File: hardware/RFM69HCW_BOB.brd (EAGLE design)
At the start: 27.9 x 20.3 mm, 11 parts, among them U1 RFM69HCW

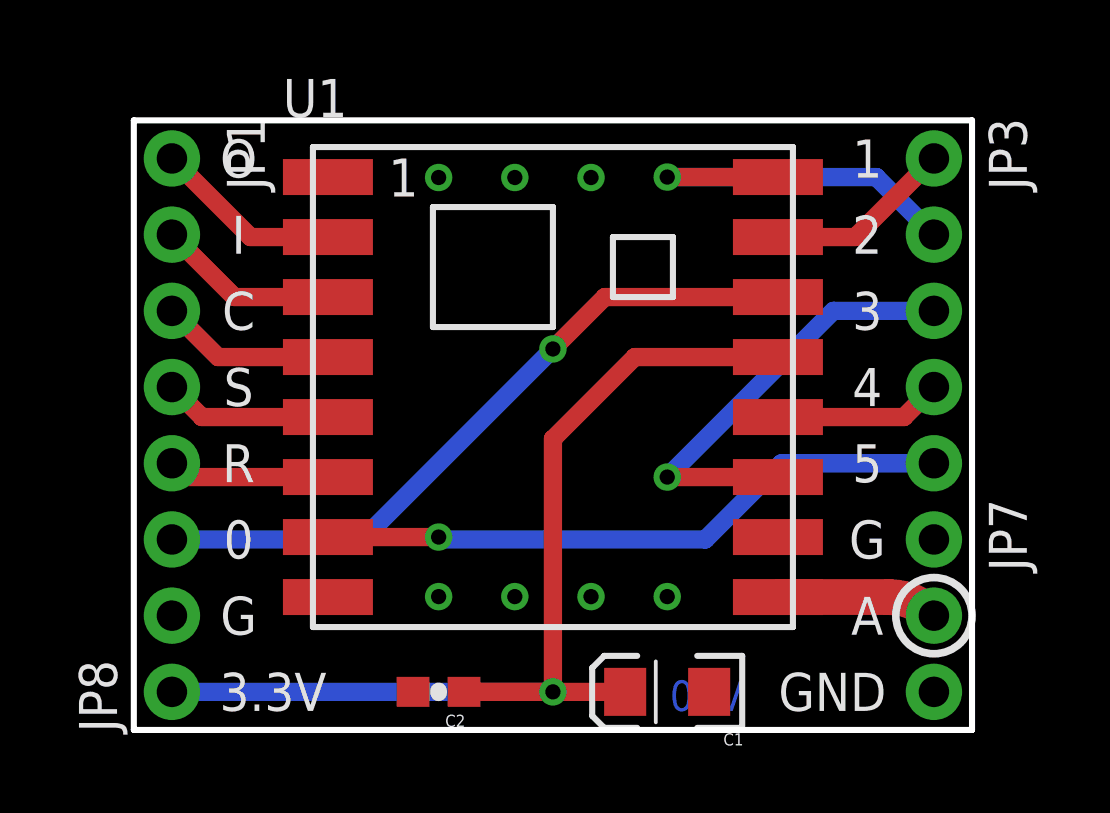
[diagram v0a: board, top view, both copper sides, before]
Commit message: Added fiducials to HCW BOB, initial example code
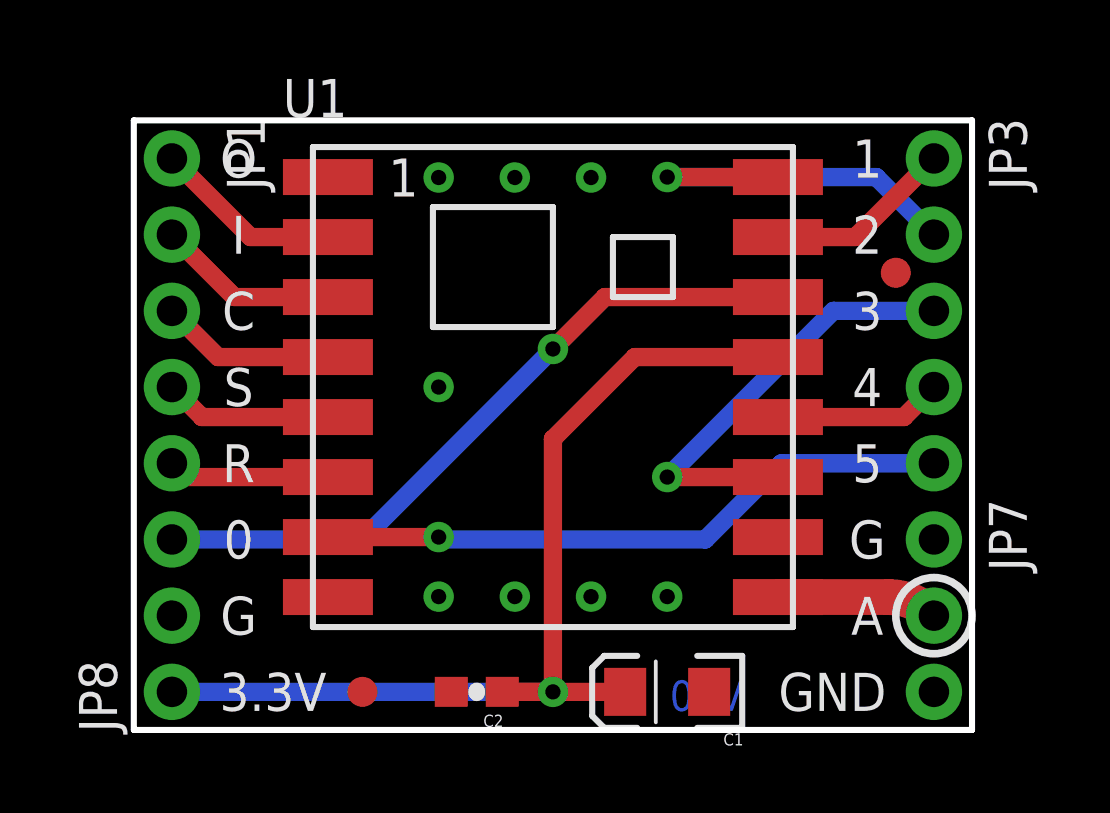
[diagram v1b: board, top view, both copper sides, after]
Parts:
- added FID1, FID2: FIDUCIAL1X2, SparkFun-Aesthetics:FIDUCIAL-1X2
- moved C2 1.27 mm to (11.4, 1.27)
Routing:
- net 3.3V: track 35.1 -> 33.9 mm
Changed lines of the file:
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@@
 <?xml version="1.0" encoding="utf-8"?>
 <!DOCTYPE eagle SYSTEM "eagle.dtd">
-<eagle version="6.4">
+<eagle version="6.5.0">
 <drawing>
 <settings>
@@
 <grid distance="0.05" unitdist="inch" unit="inch" style="lines" multiple="2" display="yes" altdistance="0.0125" altunitdist="inch" altunit="inch"/>
 <layers>
-<layer number="1" name="Top" color="4" fill="1" visible="no" active="yes"/>
+<layer number="1" name="Top" color="4" fill="1" visible="yes" active="yes"/>
 <layer number="2" name="Route2" color="1" fill="3" visible="no" active="no"/>
 <layer number="3" name="Route3" color="4" fill="3" visible="no" active="no"/>
@@
 <layer number="14" name="Route14" color="1" fill="6" visible="no" active="no"/>
 <layer number="15" name="Route15" color="4" fill="6" visible="no" active="no"/>
-<layer number="16" name="Bottom" color="1" fill="1" visible="yes" active="yes"/>
+<layer number="16" name="Bottom" color="1" fill="1" visible="no" active="yes"/>
 <layer number="17" name="Pads" color="2" fill="1" visible="yes" active="yes"/>
 <layer number="18" name="Vias" color="2" fill="1" visible="yes" active="yes"/>
 <layer number="19" name="Unrouted" color="6" fill="1" visible="yes" active="yes"/>
 <layer number="20" name="Dimension" color="15" fill="1" visible="yes" active="yes"/>
-<layer number="21" name="tPlace" color="7" fill="1" visible="no" active="yes"/>
-<layer number="22" name="bPlace" color="7" fill="1" visible="yes" active="yes"/>
-<layer number="23" name="tOrigins" color="15" fill="1" visible="no" active="yes"/>
-<layer number="24" name="bOrigins" color="15" fill="1" visible="yes" active="yes"/>
+<layer number="21" name="tPlace" color="7" fill="1" visible="yes" active="yes"/>
+<layer number="22" name="bPlace" color="7" fill="1" visible="no" active="yes"/>
+<layer number="23" name="tOrigins" color="15" fill="1" visible="yes" active="yes"/>
+<layer number="24" name="bOrigins" color="15" fill="1" visible="no" active="yes"/>
 <layer number="25" name="tNames" color="7" fill="1" visible="no" active="yes"/>
 <layer number="26" name="bNames" color="7" fill="1" visible="no" active="yes"/>
 <layer number="27" name="tValues" color="7" fill="1" visible="no" active="yes"/>
 <layer number="28" name="bValues" color="7" fill="1" visible="no" active="yes"/>
-<layer number="29" name="tStop" color="7" fill="3" visible="no" active="yes"/>
+<layer number="29" name="tStop" color="7" fill="3" visible="yes" active="yes"/>
 <layer number="30" name="bStop" color="7" fill="6" visible="no" active="yes"/>
-<layer number="31" name="tCream" color="7" fill="4" visible="no" active="yes"/>
+<layer number="31" name="tCream" color="7" fill="4" visible="yes" active="yes"/>
 <layer number="32" name="bCream" color="7" fill="5" visible="no" active="yes"/>
 <layer number="33" name="tFinish" color="6" fill="3" visible="no" active="yes"/>
@@
 </class>
 </classes>
-<designrules name="default *">
-<description language="de">&lt;b&gt;EAGLE Design Rules&lt;/b&gt;
-&lt;p&gt;
-Die Standard-Design-Rules sind so gewählt, dass sie für
-die meisten Anwendungen passen. Sollte ihre Platine
-besondere Anforderungen haben, treffen Sie die erforderlichen
-Einstellungen hier und speichern die Design Rules unter
-einem neuen Namen ab.</description>
+<designrules name="SparkFun">
 <description language="en">&lt;b&gt;EAGLE Design Rules&lt;/b&gt;
 &lt;p&gt;
@@
 <param name="mdViaViaSameLayer" value="8mil"/>
 <param name="mnLayersViaInSmd" value="2"/>
-<param name="mdCopperDimension" value="12mil"/>
+<param name="mdCopperDimension" value="8mil"/>
 <param name="mdDrill" value="8mil"/>
 <param name="mdSmdStop" value="0mil"/>
-<param name="msWidth" value="10mil"/>
-<param name="msDrill" value="24mil"/>
+<param name="msWidth" value="7mil"/>
+<param name="msDrill" value="15mil"/>
 <param name="msMicroVia" value="9.99mm"/>
 <param name="msBlindViaRatio" value="0.5"/>
@@
 <param name="rvMicroViaOuter" value="0.25"/>
 <param name="rvMicroViaInner" value="0.25"/>
-<param name="rlMinPadTop" value="10mil"/>
+<param name="rlMinPadTop" value="12mil"/>
 <param name="rlMaxPadTop" value="20mil"/>
 <param name="rlMinPadInner" value="10mil"/>
 <param name="rlMaxPadInner" value="20mil"/>
-<param name="rlMinPadBottom" value="10mil"/>
+<param name="rlMinPadBottom" value="12mil"/>
 <param name="rlMaxPadBottom" value="20mil"/>
-<param name="rlMinViaOuter" value="8mil"/>
+<param name="rlMinViaOuter" value="10mil"/>
 <param name="rlMaxViaOuter" value="20mil"/>
-<param name="rlMinViaInner" value="8mil"/>
+<param name="rlMinViaInner" value="10mil"/>
 <param name="rlMaxViaInner" value="20mil"/>
 <param name="rlMinMicroViaOuter" value="4mil"/>
@@
 <param name="mlMinCreamFrame" value="0mil"/>
 <param name="mlMaxCreamFrame" value="0mil"/>
-<param name="mlViaStopLimit" value="0mil"/>
+<param name="mlViaStopLimit" value="20mil"/>
 <param name="srRoundness" value="0"/>
 <param name="srMinRoundness" value="0mil"/>
@@
 <element name="U1" library="mike-temp" package="RFM69HCW-XXXS2" value="RFM69HCW" x="13.97" y="11.43"/>
 <element name="FRAME1" library="SparkFun-Aesthetics" package="CREATIVE_COMMONS" value="FRAME-LETTER" x="-15.24" y="-12.7"/>
-<element name="C2" library="SparkFun-Capacitors" package="0603-CAP" value="0.1uF" x="10.16" y="1.27" rot="R180">
-<attribute name="PROD_ID" value="CAP-00810" x="-5.08" y="38.1" size="1.778" layer="27" rot="R180" display="off"/>
+<element name="C2" library="SparkFun-Capacitors" package="0603-CAP" value="0.1uF" x="11.43" y="1.27" rot="R180">
+<attribute name="PROD_ID" value="CAP-00810" x="-3.81" y="38.1" size="1.778" layer="27" rot="R180" display="off"/>
 </element>
 <element name="C1" library="SparkFun-Capacitors" package="EIA3216" value="10uF" x="17.78" y="1.27" rot="R180">
@@
 <element name="JP2" library="mike-temp" package="1X01NS" value="" x="1.27" y="6.35"/>
 <element name="JP3" library="mike-temp" package="1X05_ROUNDONLY_NOSILK" value="" x="26.67" y="19.05" rot="R270"/>
+<element name="FID1" library="SparkFun-Aesthetics" package="FIDUCIAL-1X2" value="FIDUCIAL1X2" x="7.62" y="1.27"/>
+<element name="FID2" library="SparkFun-Aesthetics" package="FIDUCIAL-1X2" value="FIDUCIAL1X2" x="25.4" y="15.24"/>
 </elements>
 <signals>
@@
 <via x="15.24" y="18.415" extent="1-16" drill="0.508"/>
 <via x="10.16" y="18.415" extent="1-16" drill="0.508"/>
+<via x="10.16" y="11.43" extent="1-16" drill="0.508"/>
 </signal>
 <signal name="3.3V">
@@
 <via x="13.97" y="1.27" extent="1-16" drill="0.508"/>
 <wire x1="13.97" y1="1.27" x2="16.38" y2="1.27" width="0.6096" layer="1"/>
-<wire x1="13.97" y1="1.27" x2="11.01" y2="1.27" width="0.6096" layer="1"/>
+<wire x1="13.97" y1="1.27" x2="12.28" y2="1.27" width="0.6096" layer="1"/>
 <contactref element="JP8" pad="1"/>
 <contactref element="U1" pad="13"/>
